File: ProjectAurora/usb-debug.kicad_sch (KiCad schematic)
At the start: 20 parts, among them J1 USB_C_Receptacle_USB2.0_14P, J2 Conn_ARM_SWD_TagConnect_TC203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, U2 CP2102N-Axx-xQFN20, U3 TPD2EUSB30A

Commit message: Schematic Done
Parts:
- removed J2: Conn_ARM_SWD_TagConnect_TC2030-NL, Connector:Tag-Connect_TC2030-IDC-NL_2x03_P1.27mm_Vertical, symbol Connector:Conn_ARM_SWD_TagConnect_TC2030-NL
- added TP3, TP4, TP5, TP6, TP7: TestPoint, symbol Connector:TestPoint
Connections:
- net +3V3: now also TP3.1
- net GND: now also TP7.1
- net NRST: now also TP6.1
- net SWCLK: now also TP5.1
- net SWDIO: now also TP4.1
- no-connect marks 8 -> 7

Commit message: Starting Layout
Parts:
- C10, C11, C12, C8, C9: footprint (none) -> Capacitor_SMD:C_0603_1608Metric
- D13, D14: footprint (none) -> LED_SMD:LED_0603_1608Metric
- J1: footprint (none) -> Connector_USB:USB_C_Receptacle_GCT_USB4105-xx-A_16P_TopMnt_Horizontal
- R10, R3, R4, R5, R6, R7, R8, R9: footprint (none) -> Resistor_SMD:R_0603_1608Metric
- TP1: footprint (none) -> Test-Point-Jumper:2-Pin-Jumper; now not fitted
- TP3, TP4, TP5, TP6, TP7: footprint (none) -> TestPoint:TestPoint_Pad_D1.5mm; now not fitted
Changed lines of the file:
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@@
 			)
 		)
-		(property "Footprint" ""
+		(property "Footprint" "Capacitor_SMD:C_0603_1608Metric"
 			(at 114.3 114.6048 0)
 			(effects
@@
 			)
 		)
-		(property "Footprint" ""
+		(property "Footprint" "Connector_USB:USB_C_Receptacle_GCT_USB4105-xx-A_16P_TopMnt_Horizontal"
 			(at 180.34 87.63 0)
 			(effects
@@
 		(in_bom yes)
 		(on_board yes)
-		(dnp no)
+		(dnp yes)
 		(fields_autoplaced yes)
 		(property "Reference" "TP1"
@@
 			)
 		)
-		(property "Footprint" ""
+		(property "Footprint" "Test-Point-Jumper:2-Pin-Jumper"
 			(at 130.81 110.49 0)
 			(effects
@@
 		(in_bom yes)
 		(on_board yes)
-		(dnp no)
+		(dnp yes)
 		(fields_autoplaced yes)
 		(property "Reference" "TP5"
@@
 			)
 		)
-		(property "Footprint" ""
+		(property "Footprint" "TestPoint:TestPoint_Pad_D1.5mm"
 			(at 39.37 118.11 0)
 			(effects
@@
 		(in_bom yes)
 		(on_board yes)
-		(dnp no)
+		(dnp yes)
 		(fields_autoplaced yes)
 		(property "Reference" "TP6"
@@
 			)
 		)
-		(property "Footprint" ""
+		(property "Footprint" "TestPoint:TestPoint_Pad_D1.5mm"
 			(at 35.56 121.92 0)
 			(effects
@@
 		(in_bom yes)
 		(on_board yes)
-		(dnp no)
+		(dnp yes)
 		(fields_autoplaced yes)
 		(property "Reference" "TP4"
@@
 			)
 		)
-		(property "Footprint" ""
+		(property "Footprint" "TestPoint:TestPoint_Pad_D1.5mm"
 			(at 43.18 114.3 0)
 			(effects
@@
 			)
 		)
-		(property "Footprint" ""
+		(property "Footprint" "LED_SMD:LED_0603_1608Metric"
 			(at 92.71 55.88 0)
 			(effects
@@
 			)
 		)
-		(property "Footprint" ""
+		(property "Footprint" "Resistor_SMD:R_0603_1608Metric"
 			(at 132.842 82.55 90)
 			(effects
@@
 			)
 		)
-		(property "Footprint" ""
+		(property "Footprint" "Resistor_SMD:R_0603_1608Metric"
 			(at 137.16 107.188 90)
 			(effects
@@
 			)
 		)
-		(property "Footprint" ""
+		(property "Footprint" "Resistor_SMD:R_0603_1608Metric"
 			(at 132.842 92.71 90)
 			(effects
@@
 			)
 		)
-		(property "Footprint" ""
+		(property "Footprint" "Resistor_SMD:R_0603_1608Metric"
 			(at 165.1 96.012 90)
 			(effects
@@
 			)
 		)
-		(property "Footprint" ""
+		(property "Footprint" "Resistor_SMD:R_0603_1608Metric"
 			(at 165.1 93.472 90)
 			(effects
@@
 			)
 		)
-		(property "Footprint" ""
+		(property "Footprint" "Capacitor_SMD:C_0603_1608Metric"
 			(at 116.84 132.3848 0)
 			(effects
@@
 		(in_bom yes)
 		(on_board yes)
-		(dnp no)
+		(dnp yes)
 		(fields_autoplaced yes)
 		(property "Reference" "TP7"
@@
 			)
 		)
-		(property "Footprint" ""
+		(property "Footprint" "TestPoint:TestPoint_Pad_D1.5mm"
 			(at 31.75 125.73 0)
 			(effects
@@
 			)
 		)
-		(property "Footprint" ""
+		(property "Footprint" "Capacitor_SMD:C_0603_1608Metric"
 			(at 116.84 126.0348 0)
 			(effects
@@
 			)
 		)
-		(property "Footprint" ""
+		(property "Footprint" "Capacitor_SMD:C_0603_1608Metric"
 			(at 114.3 108.2548 0)
 			(effects
@@
 			)
 		)
-		(property "Footprint" ""
+		(property "Footprint" "LED_SMD:LED_0603_1608Metric"
 			(at 97.79 55.88 0)
 			(effects
@@
 			)
 		)
-		(property "Footprint" ""
+		(property "Footprint" "Capacitor_SMD:C_0603_1608Metric"
 			(at 201.6252 62.23 0)
 			(effects
@@
 			)
 		)
-		(property "Footprint" ""
+		(property "Footprint" "Resistor_SMD:R_0603_1608Metric"
 			(at 96.012 48.26 90)
 			(effects
@@
 		(in_bom yes)
 		(on_board yes)
-		(dnp no)
+		(dnp yes)
 		(fields_autoplaced yes)
 		(property "Reference" "TP3"
@@
 			)
 		)
-		(property "Footprint" ""
+		(property "Footprint" "TestPoint:TestPoint_Pad_D1.5mm"
 			(at 48.26 110.49 0)
 			(effects
@@
 			)
 		)
-		(property "Footprint" ""
+		(property "Footprint" "Resistor_SMD:R_0603_1608Metric"
 			(at 189.992 58.42 90)
 			(effects
@@
 			)
 		)
-		(property "Footprint" ""
+		(property "Footprint" "Resistor_SMD:R_0603_1608Metric"
 			(at 90.932 48.26 90)
 			(effects

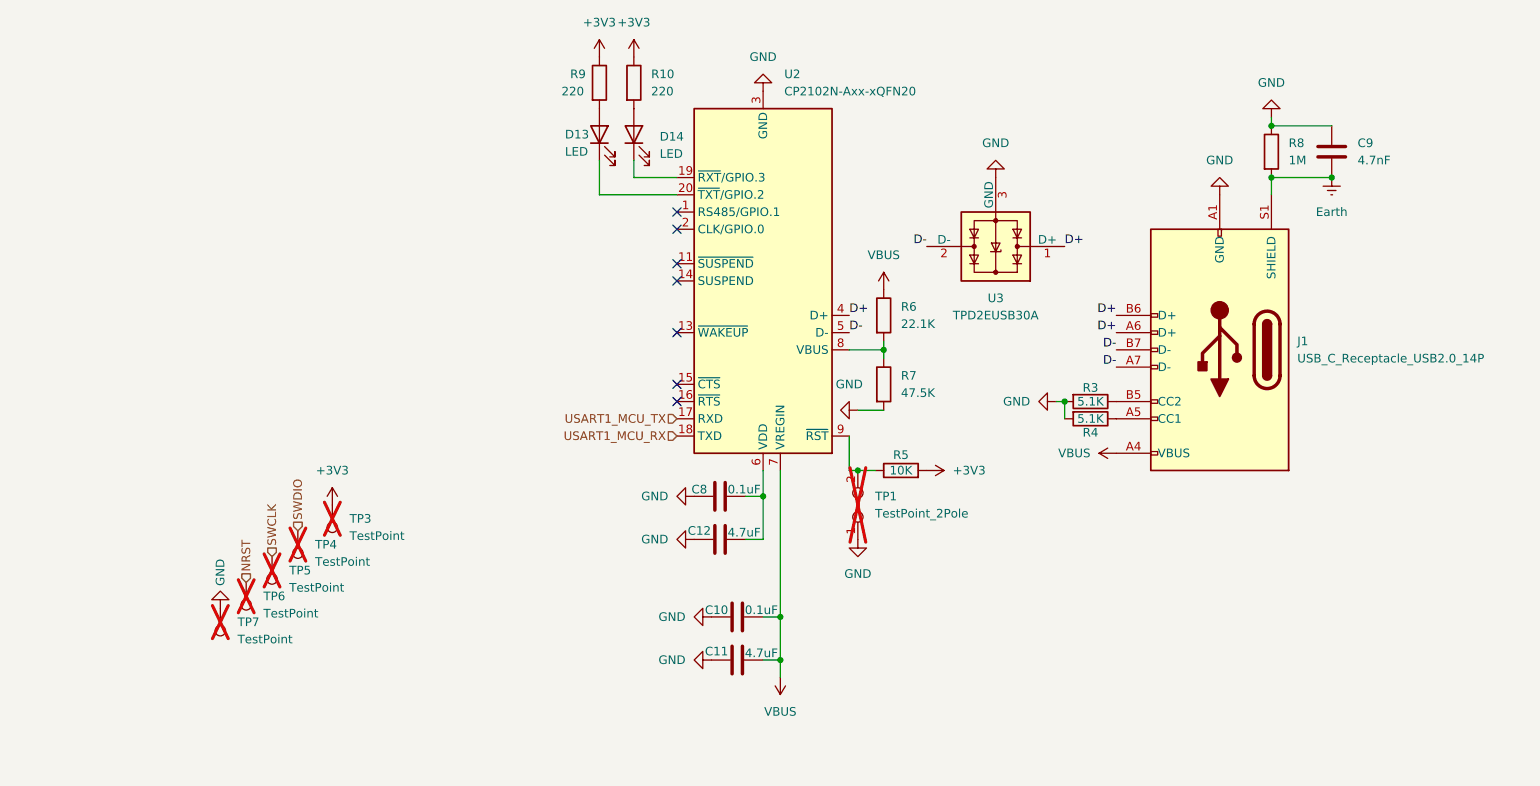
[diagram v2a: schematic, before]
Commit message: Prototype Board Layout Done
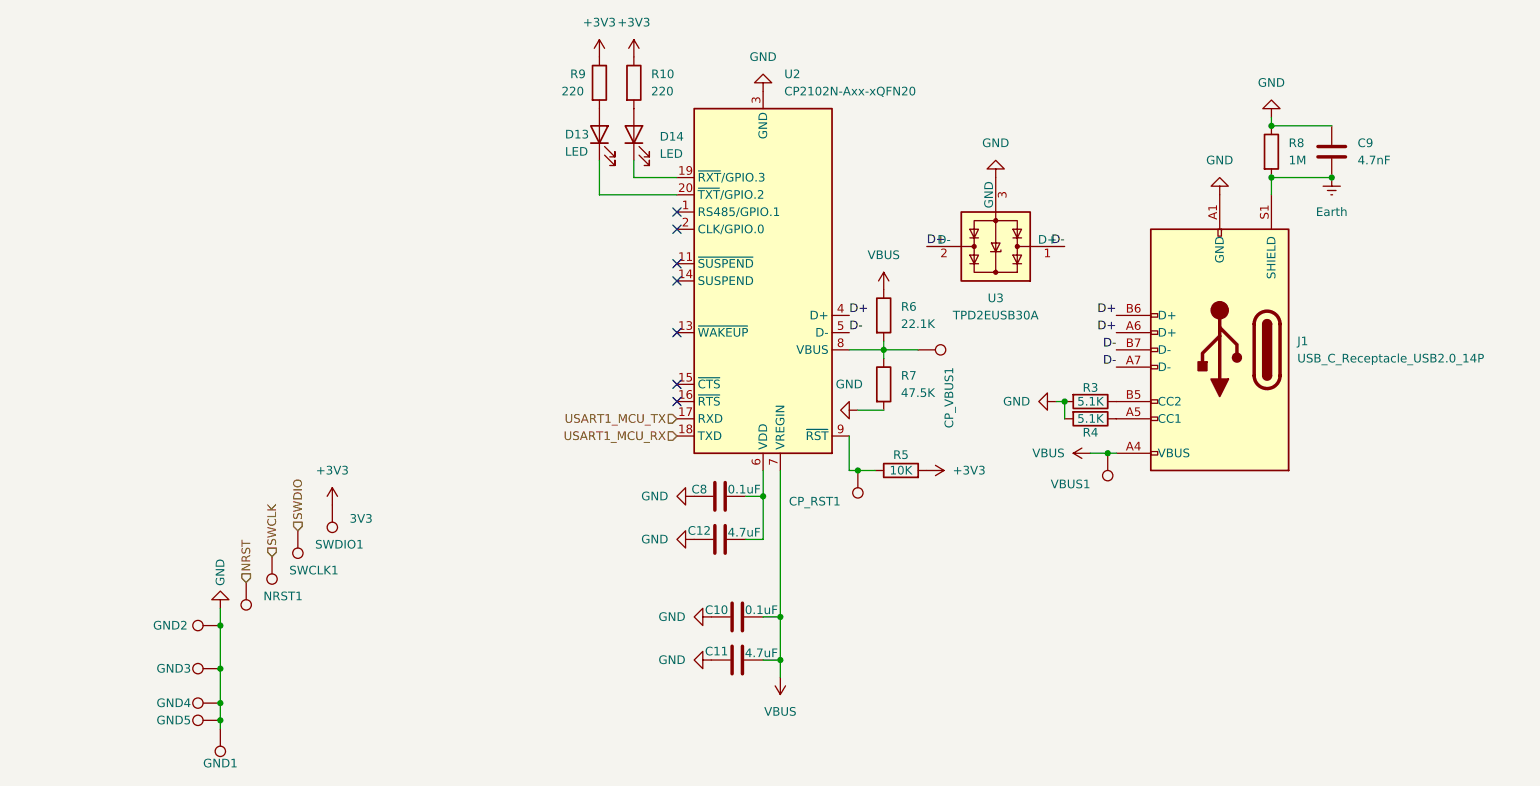
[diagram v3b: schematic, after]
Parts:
- removed TP1: TestPoint_2Pole, Test-Point-Jumper:2-Pin-Jumper, symbol Connector:TestPoint_2Pole
- added CP_RST1, CP_VBUS1, GND2, GND3, GND4, GND5, VBUS1: TestPoint, TestPoint:TestPoint_Pad_1.0x1.0mm, symbol Connector:TestPoint
- 3V3: renamed from TP3; footprint TestPoint:TestPoint_Pad_D1.5mm -> TestPoint:TestPoint_Pad_2.0x2.0mm; now fitted
- GND1: renamed from TP7; footprint TestPoint:TestPoint_Pad_D1.5mm -> TestPoint:TestPoint_Pad_2.0x2.0mm; now fitted
- NRST1: renamed from TP6; footprint TestPoint:TestPoint_Pad_D1.5mm -> TestPoint:TestPoint_Pad_1.0x1.0mm; now fitted
- SWCLK1: renamed from TP5; footprint TestPoint:TestPoint_Pad_D1.5mm -> TestPoint:TestPoint_Pad_2.0x2.0mm; now fitted
- SWDIO1: renamed from TP4; footprint TestPoint:TestPoint_Pad_D1.5mm -> TestPoint:TestPoint_Pad_2.0x2.0mm; now fitted
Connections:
- net D+: now also U3.2 (D-); no longer U3.1 (D+)
- net D-: now also U3.1 (D+); no longer U3.2 (D-)
- net GND: now also GND2.1, GND3.1, GND4.1, GND5.1
- net VBUS: now also VBUS1.1
- net at R5.1, U2.9 (~{RST}): now also CP_RST1.1
- net at R6.2, R7.1, U2.8 (VBUS): now also CP_VBUS1.1

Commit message: Prototype Board Ready for Ordering
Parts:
- R5: value 10K -> 1K
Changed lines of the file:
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@@
 			)
 		)
-		(property "Datasheet" "https://www.usb.org/sites/default/files/documents/usb_type-c.zip"
+		(property "Datasheet" "https://www.lcsc.com/datasheet/C3020560.pdf?spm=wm.sxq.inf.ggs___wm.ssy.bg.0.xh&lcsc_vid=RgNfBlVfE1ALVwYDQlhcVwZQFQVeUFUCEwQMVlIEFVExVlNRTlNfXlZRQFRcUDsOAxUeFF5JWBYZEEoKFBINSQcJGk4%3D"
 			(at 180.34 87.63 0)
 			(effects
@@
 			)
 		)
-		(property "Value" "10K"
+		(property "Value" "1K"
 			(at 137.16 105.41 90)
 			(effects
